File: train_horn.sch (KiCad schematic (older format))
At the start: 43 parts

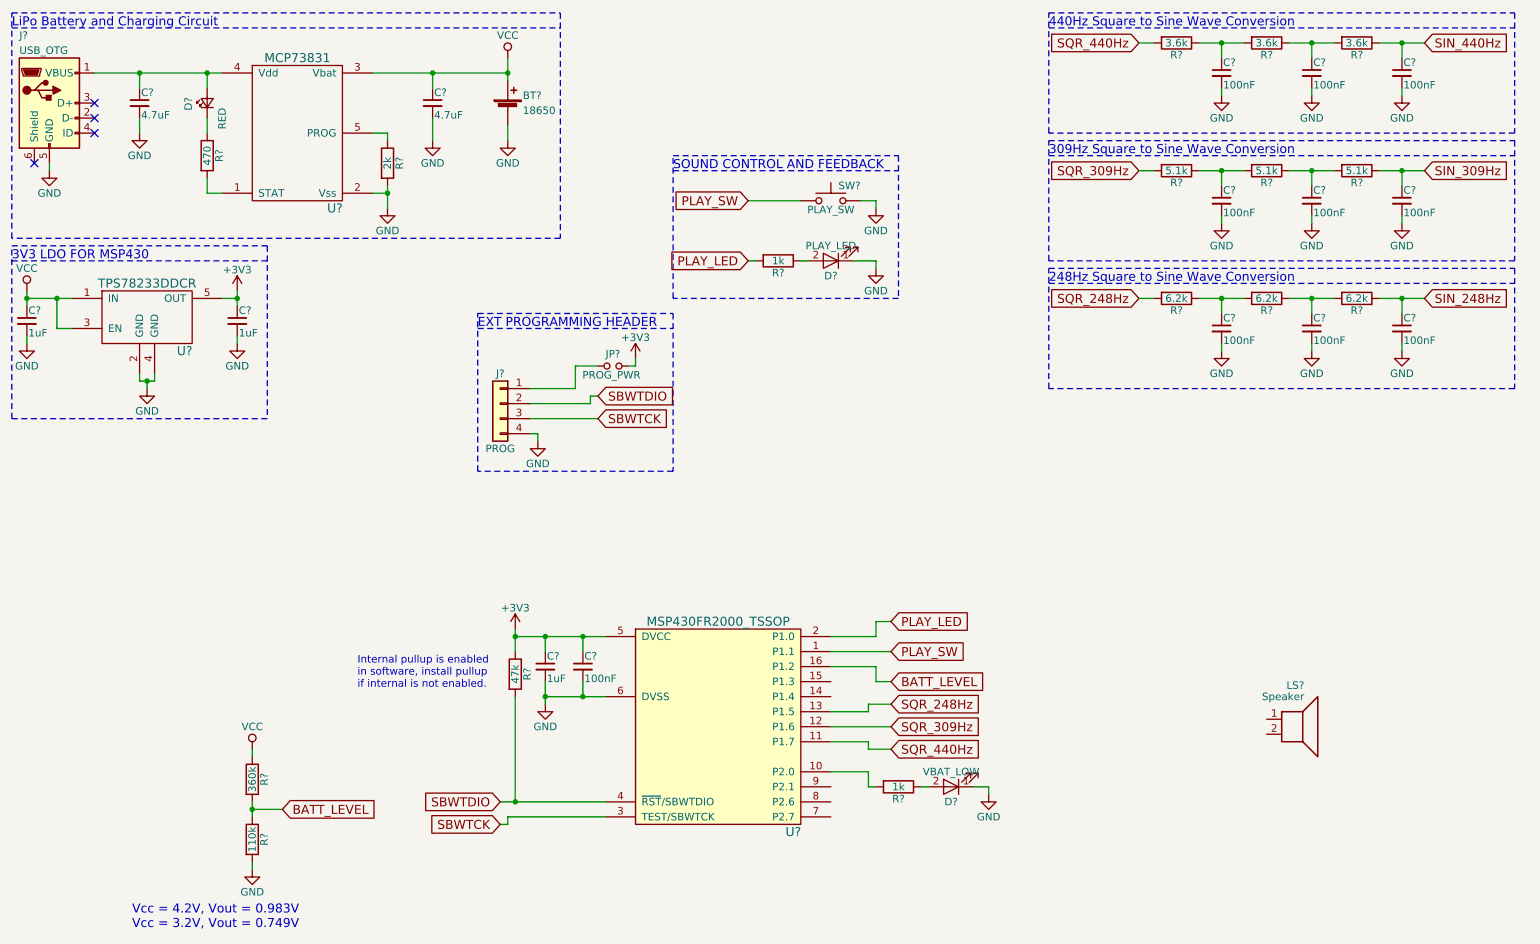
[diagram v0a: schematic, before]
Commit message: add audio amplifier to circuit rearange page layout remove comparitor references
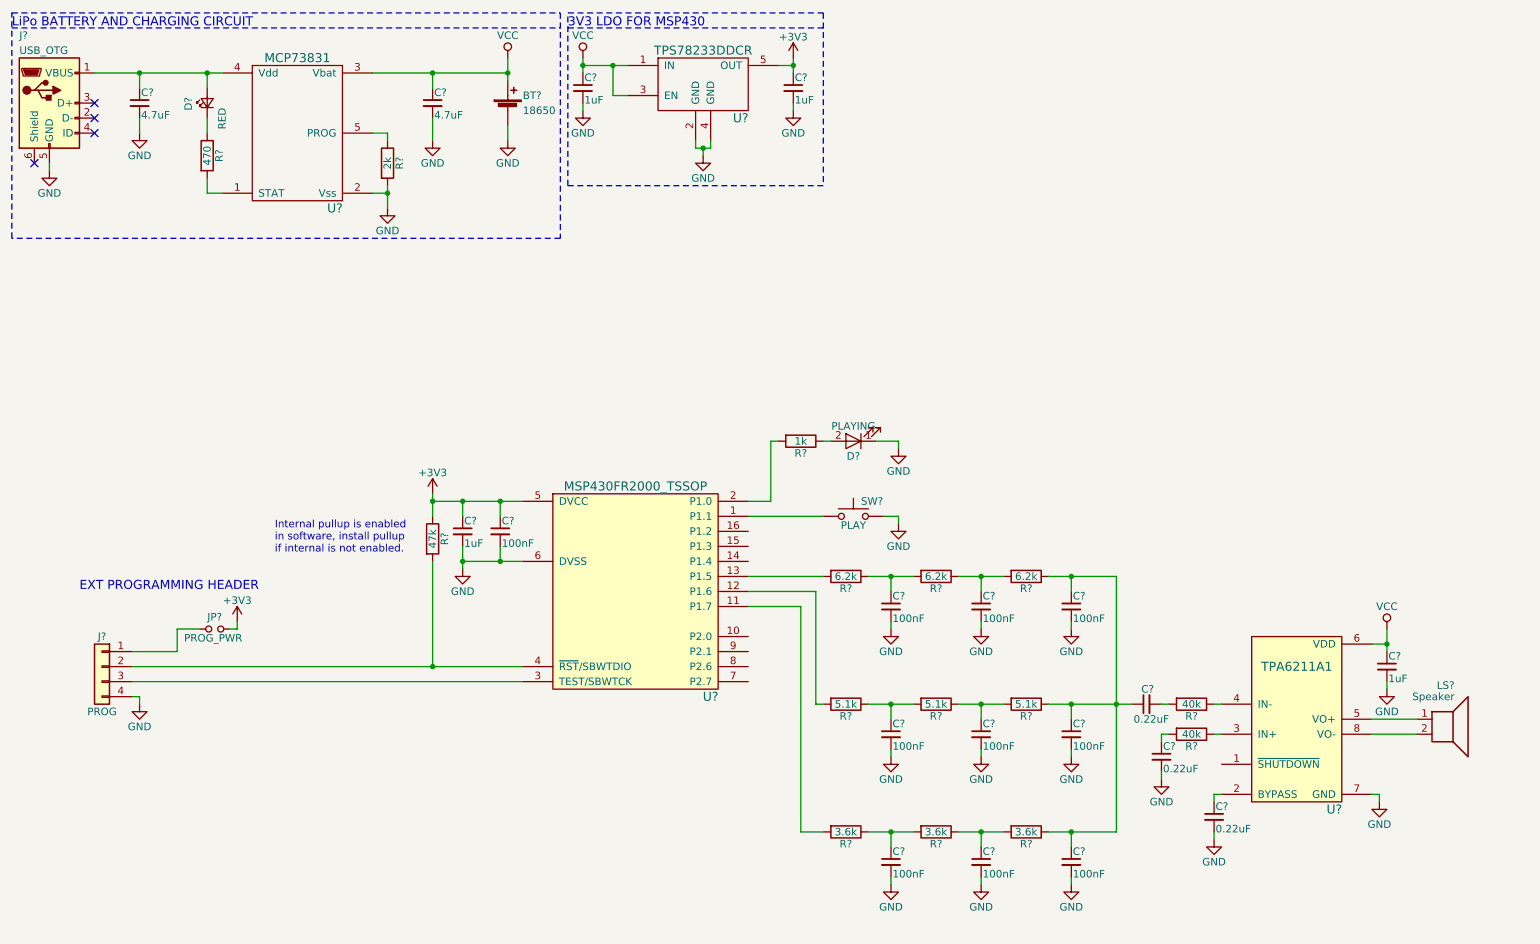
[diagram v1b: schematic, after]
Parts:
- removed D?: VBAT_LOW, symbol LED
- removed R?: 1k, symbol R
- removed R?: 360k, symbol R
- removed R?: 110k, symbol R
- added C? (x3): 0.22uF, symbol C_Small
- added C?: 1uF, symbol C_Small
- added R? (x2): 40k, symbol R
- added U?: TPA6211A1, symbol TPA6211A1
- D?: value PLAY_LED -> PLAYING
- R? (x3): value 3.6k -> 6.2k
- R? (x3): value 6.2k -> 3.6k
- SW?: value PLAY_SW -> PLAY
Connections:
- net SIN_309Hz is gone; now on an unnamed net: C?.1, R?.1
- net SIN_440Hz is gone; now on an unnamed net: C?.1, R?.1
- net GND: now also C?.2, C?.2, C?.2, U?.7 (GND)
- net VCC: now also C?.1, U?.6 (VDD)
- net at LS?.1: now also U?.5 (VO+)
- net at LS?.2: now also U?.8 (VO-)
- net BATT_LEVEL: no longer names the net of U?.16 (P1.2)
- net PLAY_LED: no longer names the net of R?.2, U?.2 (P1.0)
- net PLAY_SW: no longer names the net of SW?.1, U?.1 (P1.1)
- net SBWTCK: no longer names the net of J?.3 (Pin_3), U?.3 (TEST/SBWTCK)
- net SBWTDIO: no longer names the net of J?.2 (Pin_2), R?.2, U?.4 (~RST~/SBWTDIO)
- net SIN_248Hz: no longer names the net of C?.1, R?.1
- net SIN_248Hz: now also C?.1
- net SQR_248Hz: no longer names the net of R?.2
- net SQR_248Hz: now also U?.11 (P1.7); no longer U?.13 (P1.5)
- net SQR_309Hz: no longer names the net of R?.2, U?.12 (P1.6)
- net SQR_440Hz: no longer names the net of R?.2
- net SQR_440Hz: now also U?.13 (P1.5); no longer U?.11 (P1.7)
- new net: C?.1, U?.2 (BYPASS)
- new net: R?.1, U?.3 (IN+)
- new net: R?.1, U?.4 (IN-)
- new net: C?.2, R?.2
- new net: C?.1, R?.2
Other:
- note added: "LiPo BATTERY AND CHARGING CIRCUIT"
- note removed: "248Hz Square to Sine Wave Conversion"
- note removed: "309Hz Square to Sine Wave Conversion"
- note removed: "440Hz Square to Sine Wave Conversion"
- note removed: "LiPo Battery and Charging Circuit"
- note removed: "SOUND CONTROL AND FEEDBACK"
- note removed: "Vcc = 4.2V, Vout = 0.983V\nVcc = 3.2V, Vout = 0.749V"
- moved on the sheet: C?, D?, J?, JP?, LS?, R?, SW?, U?

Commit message: initial final schematic
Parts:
- removed R? (x2): 40k, symbol R
- added C?: 100nF, symbol C_Small
- added D?: LED, symbol LED
- added JP?: LDO_EN, symbol Jumper_NC_Small
- added JP? (x6): GADJ, symbol Jumper_NO_Small
- added Q?: 2N7002, TO_SOT_Packages_SMD:SOT-23, symbol 2N7002
- added R? (x2): 100K, symbol R
- added R?: 56K, symbol R
- added R?: 1K, symbol R
- added R? (x8): 10k, symbol R
- added TP?: P1.3, symbol Test_Point
- added TP?: P1.4, symbol Test_Point
- added TP?: P1.6, symbol Test_Point
- added TP?: P2.6, symbol Test_Point
- added TP?: P2.7, symbol Test_Point
- added U?: MIC7221, TO_SOT_Packages_SMD:SOT-23-5, symbol MCP6566R
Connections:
- net GND: now also C?.2, Q?.2 (S), R?.2, U?.5 (V-)
- net VCC: now also C?.1, JP?.2, R?.1, R?.1, R?.1, U?.2 (V+); no longer U?.3 (EN)
- net PLAY: now reaches SW?.1, U?.1 (P1.1)
- net D#4: now reaches U?.10 (P2.0)
- net D#4: now also R?.2
- net A4: now reaches R?.2
- net A4: now also U?.9 (P2.1); no longer U?.11 (P1.7)
- net at U?.12 (P1.6): now also TP?.1; no longer R?.2
- net B3: now reaches R?.2, U?.13 (P1.5)
- net at U?.14 (P1.4): now also TP?.1
- net at U?.15 (P1.3): now also TP?.1
- net ~SHDWN: now reaches U?.16 (P1.2)
- net ~SHDWN: now also U?.1 (~SHUTDOWN)
- net PLAY_LED: now reaches R?.2, U?.2 (P1.0)
- net SBWTCK: now reaches J?.3 (Pin_3), U?.3 (TEST/SBWTCK)
- net SBWTDIO: now reaches J?.2 (Pin_2), R?.2, U?.4 (~RST~/SBWTDIO)
- net at U?.7 (P2.7): now also TP?.1
- net at U?.8 (P2.6): now also TP?.1
- net at U?.3 (IN+): now also R?.1, R?.1, R?.1, R?.1
- net at U?.4 (IN-): now also R?.1, R?.1, R?.1, R?.1
- net at C?.2: now also JP?.2, R?.2
- net at C?.1: now also JP?.1, R?.2
- new net: R?.1, R?.2, U?.4 (-)
- new net: Q?.1 (G), R?.2, U?.1
- new net: D?.1 (K), Q?.3 (D)
- new net: D?.2 (A), R?.2
- new net: JP?.1, R?.2
- new net: JP?.1, JP?.2, R?.2 (x4)
- new net: JP?.2, R?.2
- new net EN: JP?.1, U?.3 (EN)
- new net VREF+: U?.11 (P1.7), U?.3 (+)
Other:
- note added: "1.2V±3.5%"
- note added: "12"
- note added: "16"
- note added: "4"
- note added: "8"
- note added: "BATTERY VOLTAGE INDICATOR"
- note added: "C"
- note added: "FREQUENCY FILTERING AND AMPLIFICATION"
- note added: "GAIN ADJUSTMENT JUMPERS"
- note added: "Gain"
- note added: "JP?"
- note added: "MSP430FR MICROCONTROLLER"
- note added: "O"
- note added: "O=OPEN\nC=CLOSED"
- note added: "See Spreadsheet for Low Battery Range"
- note added: "USER IO"
- moved on the sheet: C?, D?, J?, JP?, LS?, R?, SW?, U?

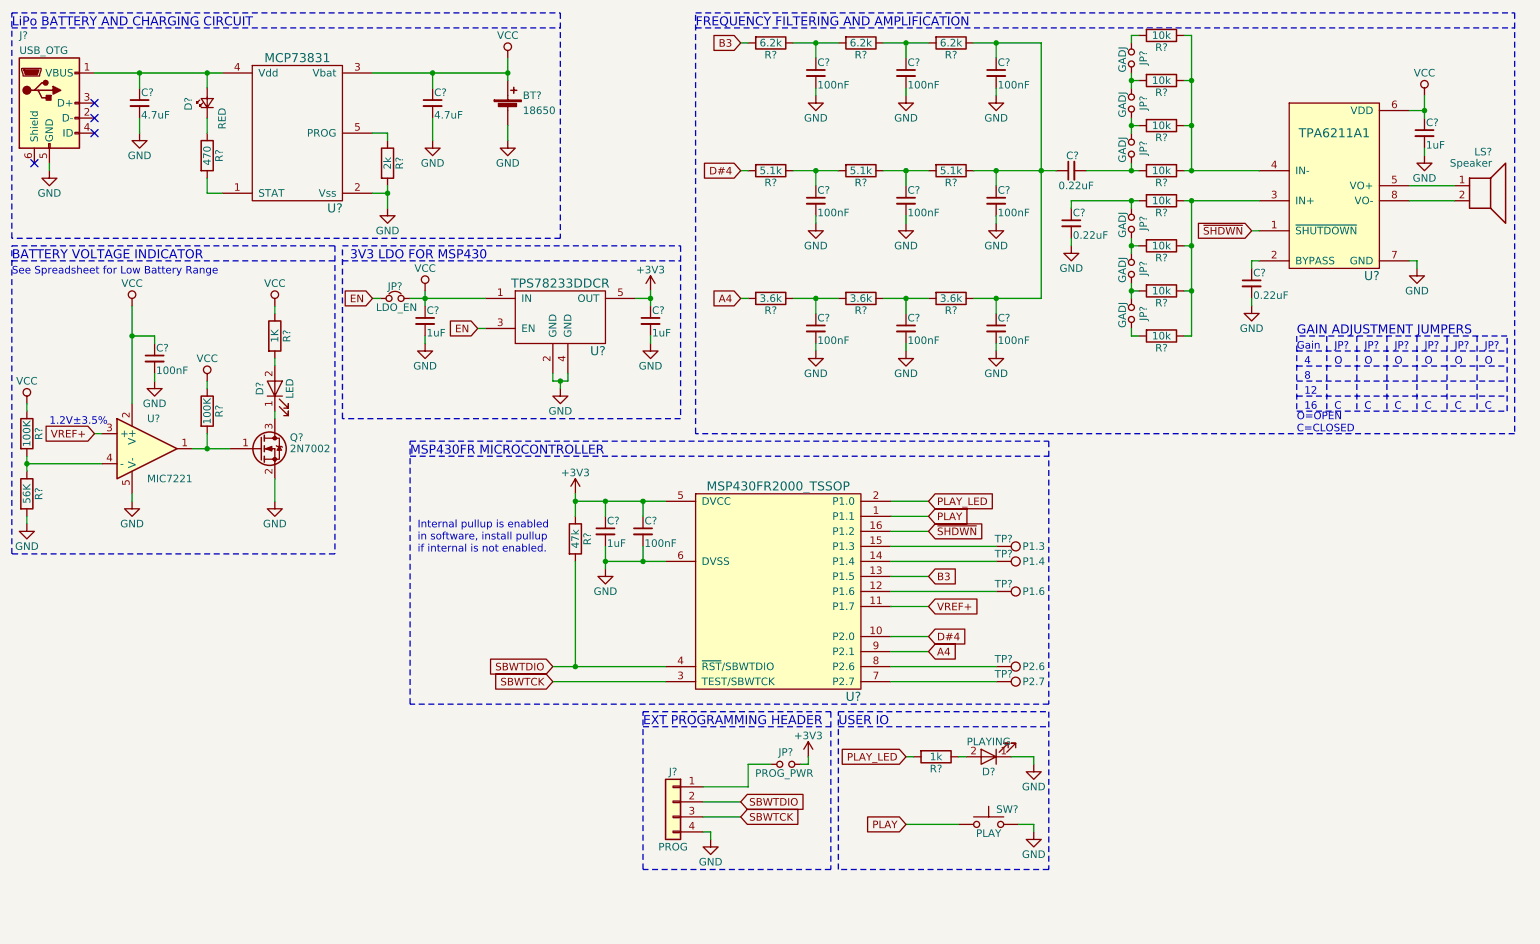
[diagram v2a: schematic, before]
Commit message: schematic annotation
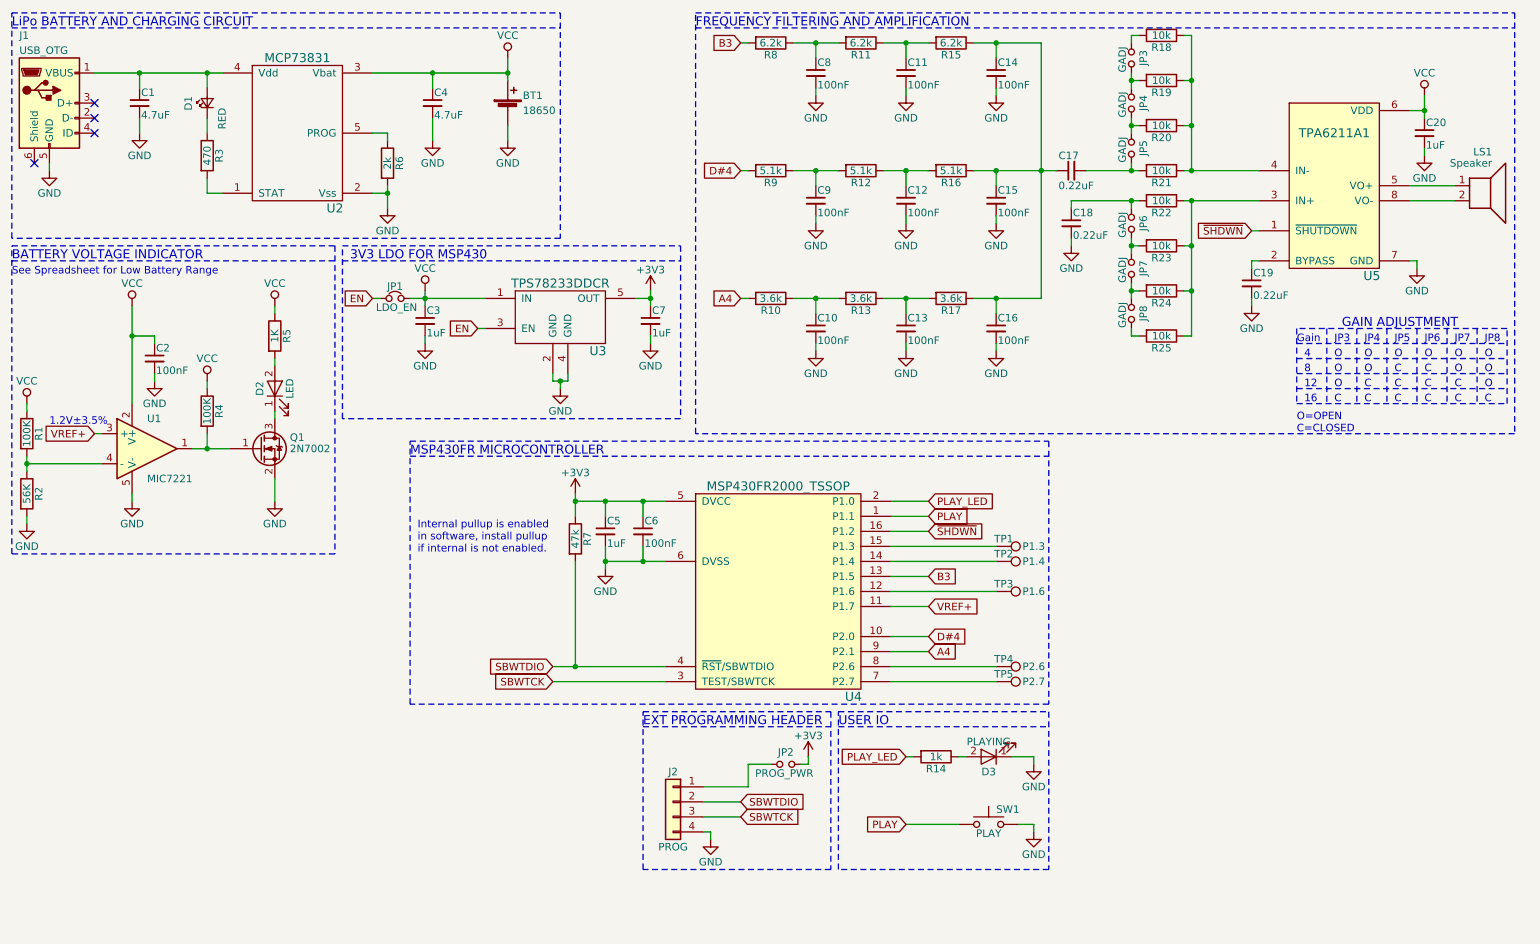
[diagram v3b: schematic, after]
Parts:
- gave numbers to parts that had none: 72
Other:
- note added: "GAIN ADJUSTMENT"
- note added: "JP3"
- note added: "JP4"
- note added: "JP5"
- note added: "JP6"
- note added: "JP7"
- note added: "JP8"
- note removed: "GAIN ADJUSTMENT JUMPERS"
- note removed: "JP?"

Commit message: swap speaker pins 1 and 2 to aid pcb layout
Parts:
- BT1: footprint (none) -> lib_fp:18650_battery_holder_PCB_Pins
- C1, C10, C11, C12, C13, C14, C15, C16, C17, C18, C19, C2, C20, C3, C4, C5, C6, C7, C8, C9: footprint (none) -> Capacitors_SMD:C_0805
- D1, D2, D3: footprint (none) -> lib_fp:LED_0805_LIGHTPIPE
- J1: footprint (none) -> Connectors_USB:USB_Micro-B_Molex_47346-0001
- J2: footprint (none) -> Pin_Headers:Pin_Header_Straight_1x04_Pitch2.54mm
- JP1, JP2, JP3, JP4, JP5, JP6, JP7, JP8: footprint (none) -> Resistors_SMD:R_1206_HandSoldering
- LS1: footprint (none) -> lib_fp:TerminalBlock_02x5mm_Straight
- R1, R10, R11, R12, R13, R14, R15, R16, R17, R18, R19, R2, R20, R21, R22, R23, R24, R25, R3, R4, R5, R6, R7, R8, R9: footprint (none) -> Resistors_SMD:R_0805
- SW1: footprint (none) -> Buttons_Switches_THT:SW_PUSH_6mm
- TP1, TP2, TP3, TP4, TP5: footprint (none) -> Connectors_TestPoints:Test_Point_Pad_d2.5mm
- U2: footprint (none) -> TO_SOT_Packages_SMD:SOT-23-5
- U3: footprint (none) -> TO_SOT_Packages_SMD:TSOT-23-5
- U4: footprint (none) -> Housings_SSOP:TSSOP-16_4.4x5mm_Pitch0.65mm
- U5: footprint (none) -> lib_fp:TPA6211A1_MSOP
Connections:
- net at LS1.1: now also U5.8 (VO-); no longer U5.5 (VO+)
- net at LS1.2: now also U5.5 (VO+); no longer U5.8 (VO-)

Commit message: setting large componet location. Change PCB size
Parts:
- TP1, TP2, TP3, TP4, TP5: footprint Connectors_TestPoints:Test_Point_Pad_d2.5mm -> Connectors_TestPoints:Test_Point_Pad_d1.5mm
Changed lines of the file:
@@
 LIBS:tps782
 LIBS:tpa6211a1
+LIBS:train_horn
 LIBS:power
 LIBS:device
@@
 F 0 "TP1" V 7000 4100 50  0000 C CNN
 F 1 "P1.3" V 7050 4300 50  0000 C CNN
-F 2 "Connectors_TestPoints:Test_Point_Pad_d2.5mm" H 7250 4050 50  0001 C CNN
+F 2 "Connectors_TestPoints:Test_Point_Pad_d1.5mm" H 7250 4050 50  0001 C CNN
 F 3 "" H 7250 4050 50  0001 C CNN
 F 4 "NONE" H 7050 4050 60  0001 C CNN "Manufacture"
@@
 F 0 "TP2" V 7000 4200 50  0000 C CNN
 F 1 "P1.4" V 7050 4400 50  0000 C CNN
-F 2 "Connectors_TestPoints:Test_Point_Pad_d2.5mm" H 7250 4150 50  0001 C CNN
+F 2 "Connectors_TestPoints:Test_Point_Pad_d1.5mm" H 7250 4150 50  0001 C CNN
 F 3 "" H 7250 4150 50  0001 C CNN
 F 4 "NONE" H 7050 4150 60  0001 C CNN "Manufacture"
@@
 F 0 "TP3" V 7000 4400 50  0000 C CNN
 F 1 "P1.6" V 7050 4600 50  0000 C CNN
-F 2 "Connectors_TestPoints:Test_Point_Pad_d2.5mm" H 7250 4350 50  0001 C CNN
+F 2 "Connectors_TestPoints:Test_Point_Pad_d1.5mm" H 7250 4350 50  0001 C CNN
 F 3 "" H 7250 4350 50  0001 C CNN
 F 4 "NONE" H 7050 4350 60  0001 C CNN "Manufacture"
@@
 F 0 "TP4" V 7000 4900 50  0000 C CNN
 F 1 "P2.6" V 7050 5100 50  0000 C CNN
-F 2 "Connectors_TestPoints:Test_Point_Pad_d2.5mm" H 7250 4850 50  0001 C CNN
+F 2 "Connectors_TestPoints:Test_Point_Pad_d1.5mm" H 7250 4850 50  0001 C CNN
 F 3 "" H 7250 4850 50  0001 C CNN
 F 4 "NONE" H 7050 4850 60  0001 C CNN "Manufacture"
@@
 F 0 "TP5" V 7000 5000 50  0000 C CNN
 F 1 "P2.7" V 7050 5200 50  0000 C CNN
-F 2 "Connectors_TestPoints:Test_Point_Pad_d2.5mm" H 7250 4950 50  0001 C CNN
+F 2 "Connectors_TestPoints:Test_Point_Pad_d1.5mm" H 7250 4950 50  0001 C CNN
 F 3 "" H 7250 4950 50  0001 C CNN
 F 4 "NONE" H 7050 4950 60  0001 C CNN "Manufacture"

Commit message: laying things out
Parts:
- J1: footprint Connectors_USB:USB_Micro-B_Molex_47346-0001 -> lib_fp:USB_Micro-B_Amphenol_10118192-0001LF
- JP2: footprint Resistors_SMD:R_1206_HandSoldering -> Pin_Headers:Pin_Header_Straight_1x02_Pitch2.54mm
- SW1: footprint Buttons_Switches_THT:SW_PUSH_6mm -> lib_fp:SWITCH_Panasonic_SMDRight_EVQP7C
- renumbered JP5 to JP3, JP3 to JP5, JP8 to JP6, JP6 to JP8
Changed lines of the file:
@@
 F 0 "J1" H 550 1550 50  0000 L CNN
 F 1 "USB_OTG" H 550 1450 50  0000 L CNN
-F 2 "Connectors_USB:USB_Micro-B_Molex_47346-0001" H 900 1050 50  0001 C CNN
+F 2 "lib_fp:USB_Micro-B_Amphenol_10118192-0001LF" H 900 1050 50  0001 C CNN
 F 3 "" H 900 1050 50  0001 C CNN
 	1    750  1100
@@
 F 0 "SW1" H 7050 6000 50  0000 L CNN
 F 1 "PLAY" H 7000 5840 50  0000 C CNN
-F 2 "Buttons_Switches_THT:SW_PUSH_6mm" H 7000 6100 50  0001 C CNN
+F 2 "lib_fp:SWITCH_Panasonic_SMDRight_EVQP7C" H 7000 6100 50  0001 C CNN
 F 3 "" H 7000 6100 50  0001 C CNN
 F 4 "NONE" H 7000 5900 60  0001 C CNN "Manufacture"
@@
 F 0 "JP2" H 5650 5580 50  0000 C CNN
 F 1 "PROG_PWR" H 5660 5440 50  0000 C CNN
-F 2 "Resistors_SMD:R_1206_HandSoldering" H 5650 5500 50  0001 C CNN
+F 2 "Pin_Headers:Pin_Header_Straight_1x02_Pitch2.54mm" H 5650 5500 50  0001 C CNN
 F 3 "" H 5650 5500 50  0001 C CNN
 F 4 "NONE" H 5650 5500 60  0001 C CNN "Manufacture"
@@
 EN
 $Comp
-L Jumper_NO_Small JP3
+L Jumper_NO_Small JP5
 U 1 1 5A832886
 P 7950 800
-F 0 "JP3" H 7950 880 50  0000 C CNN
+F 0 "JP5" H 7950 880 50  0000 C CNN
 F 1 "GADJ" H 7960 740 50  0000 C CNN
 F 2 "Resistors_SMD:R_1206_HandSoldering" H 7950 800 50  0001 C CNN
@@
 $EndComp
 $Comp
-L Jumper_NO_Small JP5
+L Jumper_NO_Small JP3
 U 1 1 5A83370F
 P 7950 1400
-F 0 "JP5" H 7950 1480 50  0000 C CNN
+F 0 "JP3" H 7950 1480 50  0000 C CNN
 F 1 "GADJ" H 7960 1340 50  0000 C CNN
 F 2 "Resistors_SMD:R_1206_HandSoldering" H 7950 1400 50  0001 C CNN
@@
 $EndComp
 $Comp
-L Jumper_NO_Small JP6
+L Jumper_NO_Small JP8
 U 1 1 5A83A0B3
 P 7950 1900
-F 0 "JP6" H 7950 1980 50  0000 C CNN
+F 0 "JP8" H 7950 1980 50  0000 C CNN
 F 1 "GADJ" H 7960 1840 50  0000 C CNN
 F 2 "Resistors_SMD:R_1206_HandSoldering" H 7950 1900 50  0001 C CNN
@@
 $EndComp
 $Comp
-L Jumper_NO_Small JP8
+L Jumper_NO_Small JP6
 U 1 1 5A83A0DB
 P 7950 2500
-F 0 "JP8" H 7950 2580 50  0000 C CNN
+F 0 "JP6" H 7950 2580 50  0000 C CNN
 F 1 "GADJ" H 7960 2440 50  0000 C CNN
 F 2 "Resistors_SMD:R_1206_HandSoldering" H 7950 2500 50  0001 C CNN
